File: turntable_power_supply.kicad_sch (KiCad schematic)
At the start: 30 parts, among them IC15 171032401, IC235 171032401, IC5 171032401, X15 694106301002, X235 694106301002, X24 694106301002, X5 PRT-21570

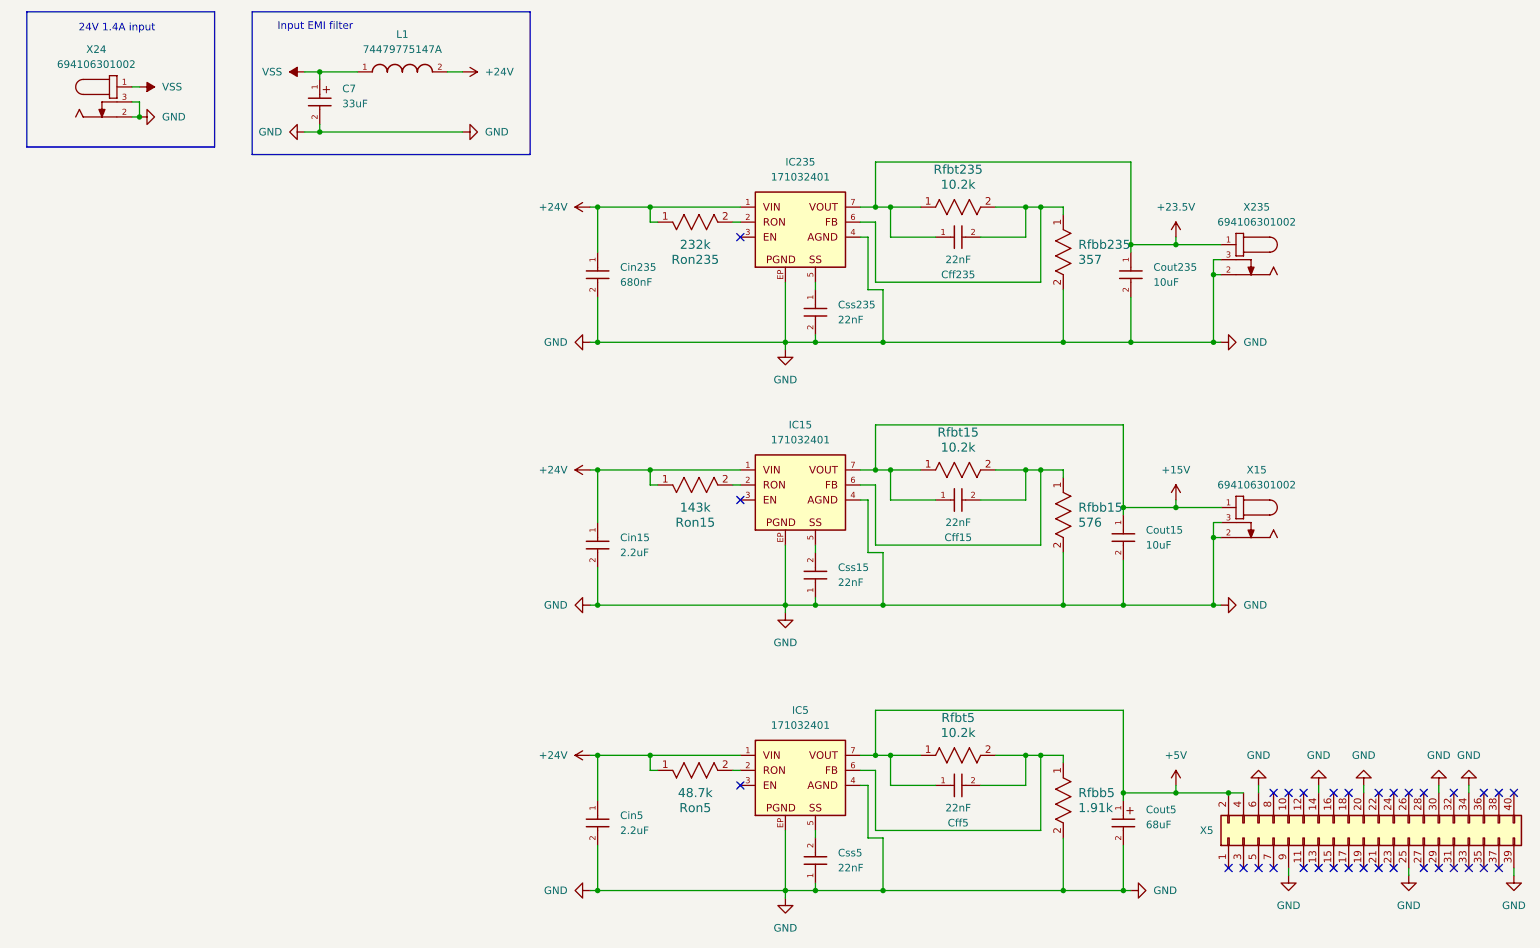
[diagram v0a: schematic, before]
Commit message: Add missing capacitors
Signed-off-by: Marc 'risson' Schmitt <marc.schmitt@risson.space>
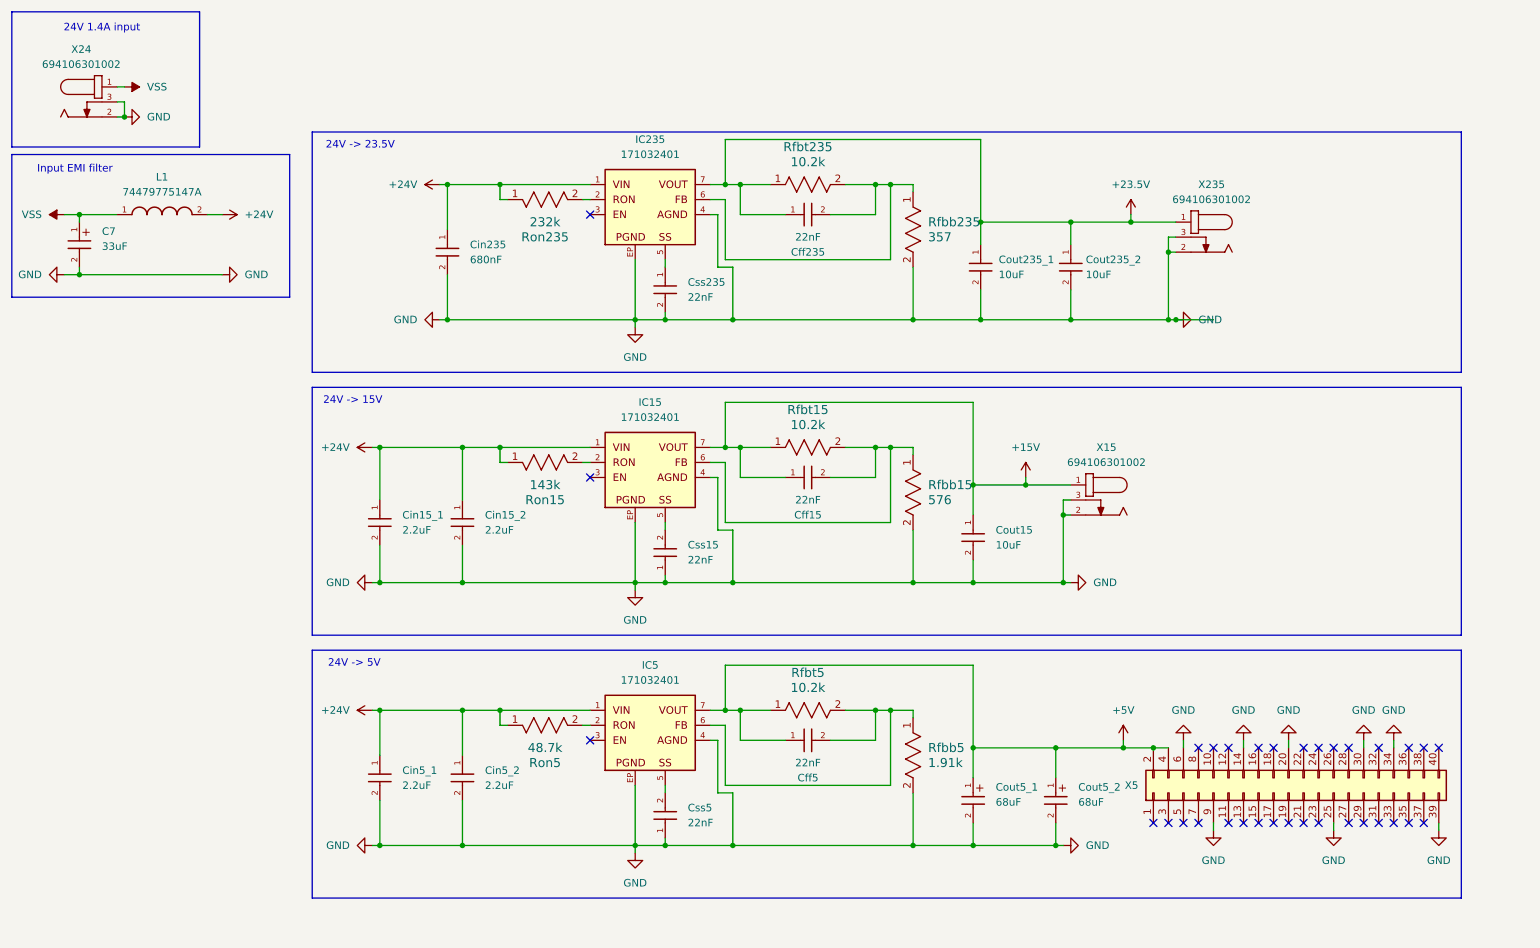
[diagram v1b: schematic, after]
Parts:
- added Cin15_2, Cin5_2: 2.2uF, 885012210032:885012210032, symbol 885012210032:885012210032
- added Cout235_2: 10uF, 885012214006:885012214006, symbol 885012214006:885012214006
- added Cout5_2: 68uF, 870235674004:870235674004, symbol 870235674004:870235674004
- renumbered Cin15 to Cin15_1, Cin5 to Cin5_1, Cout235 to Cout235_1, Cout5 to Cout5_1
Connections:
- net +23.5V: now also Cout235_2.1
- net +24V: now also Cin15_2.1, Cin5_2.1
- net +5V: now also Cout5_2.1
- net GND: now also Cin15_2.2, Cin5_2.2, Cout235_2.2, Cout5_2.2
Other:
- note added: "24V -> 15V"
- note added: "24V -> 23.5V"
- note added: "24V -> 5V"
- moved on the sheet: C7, Cff15, Cff235, Cff5, Cin15_1, Cin235, Cin5_1, Cout15, Cout235_1, Cout5_1, Css15, Css235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

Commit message: Fix Cout_15 footprint
Signed-off-by: Marc 'risson' Schmitt <marc.schmitt@risson.space>
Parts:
- Cout15: footprint 885012214006:885012214006 -> 885012214005:885012214005
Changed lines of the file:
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@@
 			)
 		)
-		(property "Footprint" "885012214006:885012214006"
+		(property "Footprint" "885012214005:885012214005"
 			(at 176.53 100.33 0)
 			(effects
